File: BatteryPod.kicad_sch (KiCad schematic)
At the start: 15 parts, among them J1 Conn_01x02_Pin, U1 LM5157RTER

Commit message: feat: almost full initial routing
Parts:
- removed J1: Conn_01x02_Pin, Connector_PinHeader_2.54mm:PinHeader_1x02_P2.54mm_Vertical, symbol Connector:Conn_01x02_Pin
- added C8: 100uF, Capacitor_SMD:CP_Elec_16x17.5, symbol Device:C_Polarized
- added H1, H2, H3, H4: MountingHole, MountingHole:MountingHole_2.5mm, symbol Mechanical:MountingHole
- added J1: VIN, Connector_Wire:SolderWire-1.5sqmm_1x02_P7.8mm_D1.7mm_OD3.9mm, symbol Connector:Conn_01x02_Socket
- C2: footprint Capacitor_SMD:C_0603_1608Metric -> Capacitor_SMD:C_2220_5750Metric
- C6: Part C426635 -> C107086
- C7: Part C2986269 -> C307347
- R1: Part (none) -> C234251
- R2: Part (none) -> C491121
- R4: Part C705949 -> C218107
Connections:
- net +BATT: now also J1.1 (Pin_1)
- net GND: now also C8.2, J1.2 (Pin_2)
- net VCC: now reaches C1.1, C4.1, D1.1 (K), R1.1
- net VCC: now also C8.1

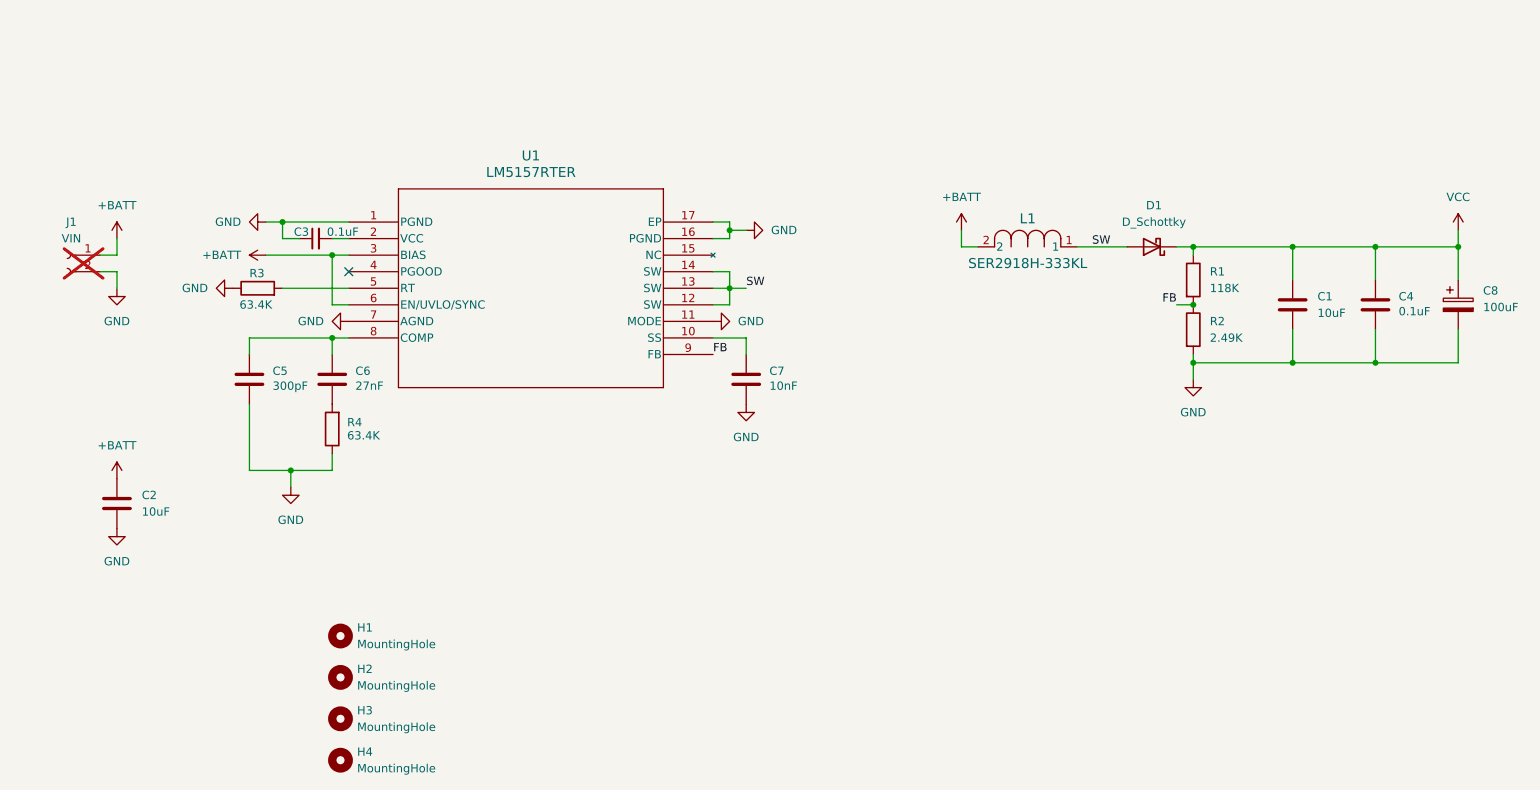
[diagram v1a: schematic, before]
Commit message: feat: correct screw positioning (hopefully)
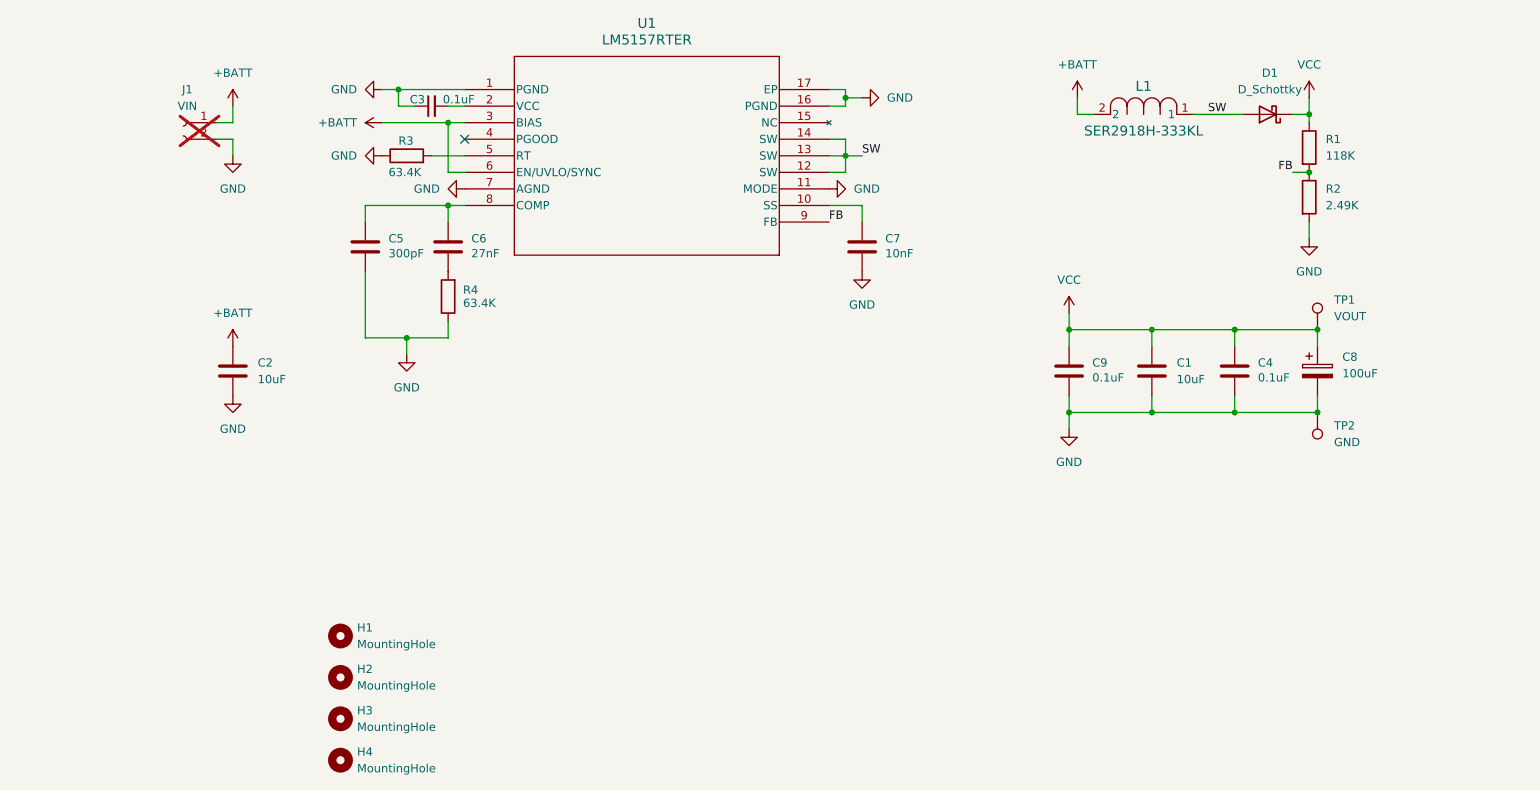
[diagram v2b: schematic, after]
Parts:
- added C9: 0.1uF, Capacitor_SMD:C_0603_1608Metric, symbol Device:C
- added TP1: VOUT, TestPoint:TestPoint_Loop_D2.50mm_Drill1.0mm_LowProfile, symbol Connector:TestPoint
- added TP2: GND, TestPoint:TestPoint_Loop_D2.50mm_Drill1.0mm_LowProfile, symbol Connector:TestPoint
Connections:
- net GND: now also C9.2, TP2.1
- net VCC: now also C9.1, TP1.1
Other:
- moved on the sheet: C2, C3, C5, C6, C7, D1, J1, L1, R1, R2, R3, R4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

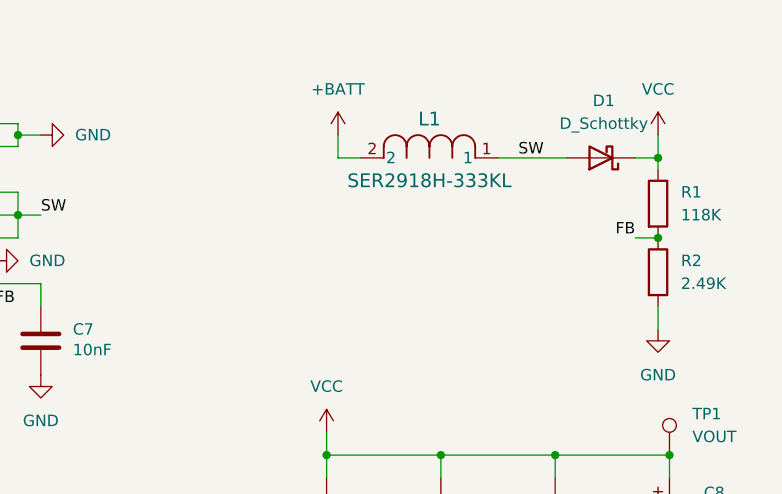
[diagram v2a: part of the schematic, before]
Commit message: patch: silkscreen improvements fix: screw hole position
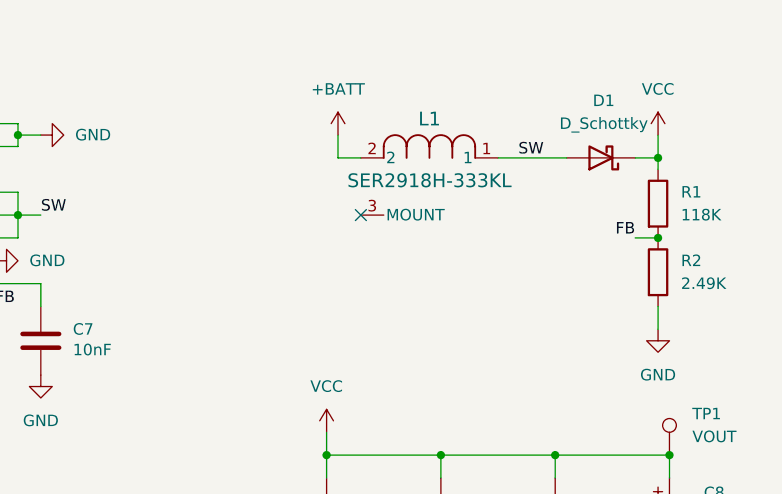
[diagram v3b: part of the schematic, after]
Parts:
- L1: footprint coilcraft-ser2918h:IND_SER2918H_COC -> IND_SER2918H_COC
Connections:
- no-connect marks 1 -> 2
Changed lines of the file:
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@@
 		(at 105.41 83.82)
+	)
+	(no_connect
+		(at 201.93 86.36)
 	)
 	(wire
@@
 			)
 		)
-		(property "Footprint" "coilcraft-ser2918h:IND_SER2918H_COC"
+		(property "Footprint" "IND_SER2918H_COC"
 			(at 201.93 80.01 0)
 			(effects
@@
 		(pin "1"
 		)
+		(pin "3"
+		)
 		(instances

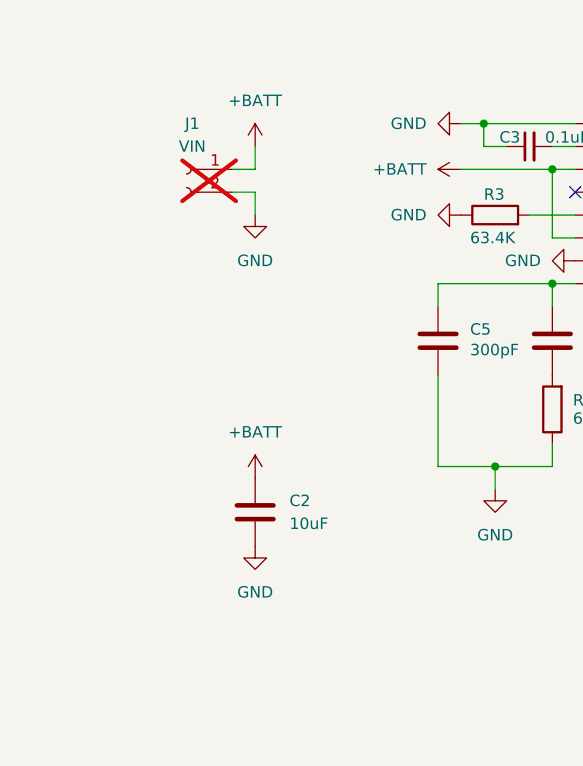
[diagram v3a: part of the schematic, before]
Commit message: feat: move to lower half of board due to high profile inductor this is to match with a recess in the chassis for the higher profile component
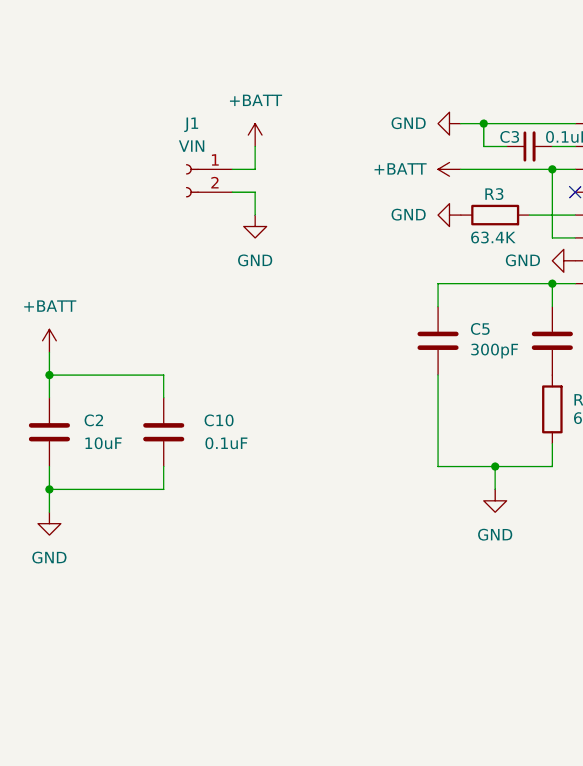
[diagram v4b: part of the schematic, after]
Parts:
- added C10: 0.1uF, Capacitor_SMD:C_0603_1608Metric, symbol Device:C
- C8: footprint Capacitor_SMD:CP_Elec_16x17.5 -> Capacitor_SMD:CP_Elec_10x10; Part C445445 -> C487156
- J1: now fitted; now left out of the parts list
- TP1, TP2: now left out of the parts list
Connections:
- net +BATT: now also C10.2
- net GND: now also C10.1
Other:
- moved on the sheet: C2
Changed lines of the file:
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@@
 	(paper "A4")
 	(junction
+		(at 46.99 104.14)
+		(diameter 0)
+		(color 0 0 0 0)
+	)
+	(junction
 		(at 210.82 125.73)
 		(diameter 0)
@@
 	)
 	(junction
+		(at 46.99 116.84)
+		(diameter 0)
+		(color 0 0 0 0)
+	)
+	(junction
 		(at 210.82 113.03)
 		(diameter 0)
@@
 	(wire
 		(pts
+			(xy 46.99 119.38) (xy 46.99 116.84)
+		)
+		(stroke
+			(width 0)
+			(type default)
+		)
+	)
+	(wire
+		(pts
 			(xy 198.12 110.49) (xy 198.12 113.03)
 		)
@@
 	(wire
 		(pts
+			(xy 46.99 101.6) (xy 46.99 104.14)
+		)
+		(stroke
+			(width 0)
+			(type default)
+		)
+	)
+	(wire
+		(pts
 			(xy 198.12 125.73) (xy 210.82 125.73)
 		)
@@
 	(wire
 		(pts
+			(xy 59.69 116.84) (xy 59.69 114.3)
+		)
+		(stroke
+			(width 0)
+			(type default)
+		)
+	)
+	(wire
+		(pts
 			(xy 234.95 80.01) (xy 234.95 81.28)
 		)
@@
 	(wire
 		(pts
+			(xy 46.99 104.14) (xy 46.99 106.68)
+		)
+		(stroke
+			(width 0)
+			(type default)
+		)
+	)
+	(wire
+		(pts
 			(xy 232.41 88.9) (xy 234.95 88.9)
 		)
@@
 	(wire
 		(pts
+			(xy 59.69 104.14) (xy 59.69 106.68)
+		)
+		(stroke
+			(width 0)
+			(type default)
+		)
+	)
+	(wire
+		(pts
 			(xy 236.22 123.19) (xy 236.22 125.73)
 		)
@@
 	(wire
 		(pts
+			(xy 46.99 116.84) (xy 59.69 116.84)
+		)
+		(stroke
+			(width 0)
+			(type default)
+		)
+	)
+	(wire
+		(pts
 			(xy 210.82 115.57) (xy 210.82 113.03)
 		)
@@
 	(wire
 		(pts
+			(xy 46.99 104.14) (xy 59.69 104.14)
+		)
+		(stroke
+			(width 0)
+			(type default)
+		)
+	)
+	(wire
+		(pts
 			(xy 163.83 78.74) (xy 163.83 77.47)
 		)
@@
 	(wire
 		(pts
+			(xy 46.99 116.84) (xy 46.99 114.3)
+		)
+		(stroke
+			(width 0)
+			(type default)
+		)
+	)
+	(wire
+		(pts
 			(xy 163.83 83.82) (xy 161.29 83.82)
 		)
@@
 	(symbol
 		(lib_id "Device:C")
-		(at 69.85 119.38 0)
+		(at 46.99 110.49 0)
 		(unit 1)
 		(exclude_from_sim no)
@@
 		(fields_autoplaced yes)
 		(property "Reference" "C2"
-			(at 73.66 118.1099 0)
+			(at 50.8 109.2199 0)
 			(effects
 				(font
@@
 		)
 		(property "Value" "10uF"
-			(at 73.66 120.6499 0)
+			(at 50.8 111.7599 0)
 			(effects
 				(font
@@
 		)
 		(property "Footprint" "Capacitor_SMD:C_2220_5750Metric"
-			(at 70.8152 123.19 0)
+			(at 47.9552 114.3 0)
 			(effects
 				(font
@@
 		)
 		(property "Datasheet" "~"
-			(at 69.85 119.38 0)
+			(at 46.99 110.49 0)
 			(effects
 				(font
@@
 		)
 		(property "Description" "Unpolarized capacitor"
-			(at 69.85 119.38 0)
+			(at 46.99 110.49 0)
 			(effects
 				(font
@@
 		)
 		(property "Part" "C342280"
-			(at 69.85 119.38 0)
+			(at 46.99 110.49 0)
 			(effects
 				(font
@@
 		)
 		(property "Part#" ""
-			(at 69.85 119.38 0)
+			(at 46.99 110.49 0)
 			(effects
 				(font
@@
 		(unit 1)
 		(exclude_from_sim no)
-		(in_bom yes)
+		(in_bom no)
 		(on_board yes)
 		(dnp no)
@@
 			)
 		)
-		(property "Part#" ""
-			(at 100.33 78.74 0)
-			(effects
-				(font
-					(size 1.27 1.27)
-				)
-				(hide yes)
-			)
-		)
 		(pin "1"
 		)
@@
 		(unit 1)
 		(exclude_from_sim no)
-		(in_bom yes)
+		(in_bom no)
 		(on_board yes)
-		(dnp yes)
+		(dnp no)
 		(fields_autoplaced yes)
 		(property "Reference" "J1"
@@
 		(unit 1)
 		(exclude_from_sim no)
-		(in_bom yes)
+		(in_bom no)
 		(on_board yes)
 		(dnp no)
@@
 	(symbol
 		(lib_id "power:+BATT")
-		(at 69.85 115.57 0)
+		(at 46.99 101.6 0)
 		(unit 1)
 		(exclude_from_sim no)
@@
 		(fields_autoplaced yes)
 		(property "Reference" "#PWR010"
-			(at 69.85 119.38 0)
+			(at 46.99 105.41 0)
 			(effects
 				(font
@@
 		)
 		(property "Value" "+BATT"
-			(at 69.85 110.49 0)
+			(at 46.99 96.52 0)
 			(effects
 				(font
@@
 		)
 		(property "Footprint" ""
-			(at 69.85 115.57 0)
+			(at 46.99 101.6 0)
 			(effects
 				(font
@@
 		)
 		(property "Datasheet" ""
-			(at 69.85 115.57 0)
+			(at 46.99 101.6 0)
 			(effects
 				(font
@@
 		)
 		(property "Description" "Power symbol creates a global label with name \"+BATT\""
-			(at 69.85 115.57 0)
+			(at 46.99 101.6 0)
 			(effects
 				(font
@@
 	(symbol
 		(lib_id "power:GND")
-		(at 69.85 123.19 0)
+		(at 46.99 119.38 0)
 		(unit 1)
 		(exclude_from_sim no)
@@
 		(fields_autoplaced yes)
 		(property "Reference" "#PWR011"
-			(at 69.85 129.54 0)
+			(at 46.99 125.73 0)
 			(effects
 				(font
@@
 		)
 		(property "Value" "GND"
-			(at 69.85 128.27 0)
+			(at 46.99 124.46 0)
 			(effects
 				(font
@@
 		)
 		(property "Footprint" ""
-			(at 69.85 123.19 0)
+			(at 46.99 119.38 0)
 			(effects
 				(font
@@
 		)
 		(property "Datasheet" ""
-			(at 69.85 123.19 0)
+			(at 46.99 119.38 0)
 			(effects
 				(font
@@
 		)
 		(property "Description" "Power symbol creates a global label with name \"GND\" , ground"
-			(at 69.85 123.19 0)
+			(at 46.99 119.38 0)
 			(effects
 				(font
@@
 	)
 	(symbol
+		(lib_id "Device:C")
+		(at 59.69 110.49 180)
+		(unit 1)
+		(exclude_from_sim no)
+		(in_bom yes)
+		(on_board yes)
+		(dnp no)
+		(property "Reference" "C10"
+			(at 67.564 109.22 0)
+			(effects
+				(font
+					(size 1.27 1.27)
+				)
+				(justify left)
+			)
+		)
+		(property "Value" "0.1uF"
+			(at 69.088 111.76 0)
+			(effects
+				(font
+					(size 1.27 1.27)
+				)
+				(justify left)
+			)
+		)
+		(property "Footprint" "Capacitor_SMD:C_0603_1608Metric"
+			(at 58.7248 106.68 0)
+			(effects
+				(font
+					(size 1.27 1.27)
+				)
+				(hide yes)
+			)
+		)
+		(property "Datasheet" "~"
+			(at 59.69 110.49 0)
+			(effects
+				(font
+					(size 1.27 1.27)
+				)
+				(hide yes)
+			)
+		)
+		(property "Description" "Unpolarized capacitor"
+			(at 59.69 110.49 0)
+			(effects
+				(font
+					(size 1.27 1.27)
+				)
+				(hide yes)
+			)
+		)
+		(property "Part" "C597287"
+			(at 59.69 110.49 90)
+			(effects
+				(font
+					(size 1.27 1.27)
+				)
+				(hide yes)
+			)
+		)
+		(pin "1"
+		)
+		(pin "2"
+		)
+		(instances
+			(project "BatteryPod"
+				(path "/4321c496-0c88-4f4f-a1d3-dd2bca7d98aa"
+					(reference "C10")
+					(unit 1)
+				)
+			)
+		)
+	)
+	(symbol
 		(lib_id "Device:D_Schottky")
 		(at 228.6 80.01 180)
@@
 			)
 		)
-		(property "Footprint" "Capacitor_SMD:CP_Elec_16x17.5"
+		(property "Footprint" "Capacitor_SMD:CP_Elec_10x10"
 			(at 237.1852 123.19 0)
 			(effects
@@
 			)
 		)
-		(property "Part" "C445445"
-			(at 236.22 119.38 0)
-			(effects
-				(font
-					(size 1.27 1.27)
-				)
-				(hide yes)
-			)
-		)
-		(property "Part#" ""
+		(property "Part" "C487156"
 			(at 236.22 119.38 0)
 			(effects

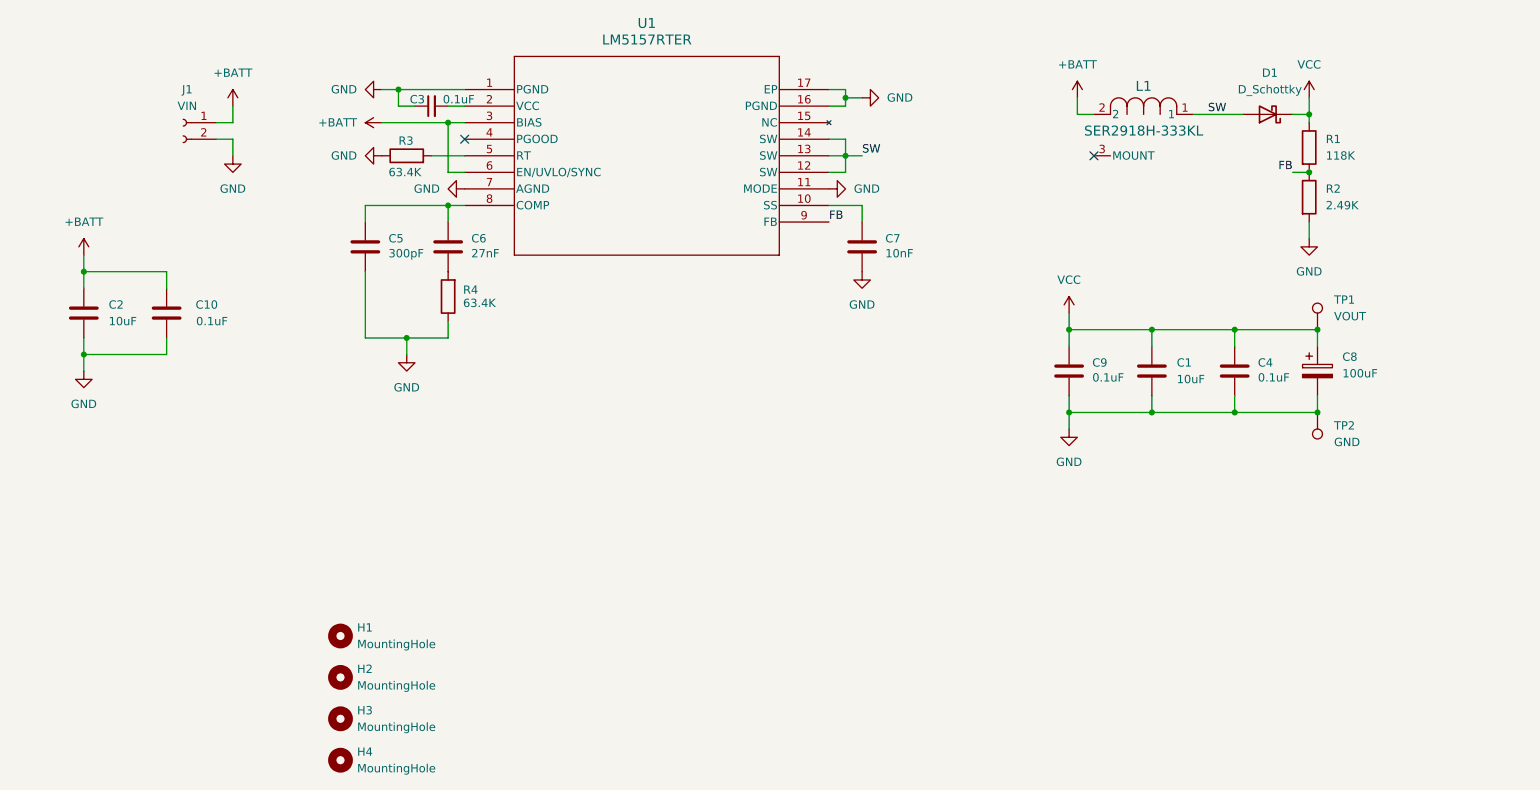
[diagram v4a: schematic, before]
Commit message: feat: add partial USB-PD input, routing
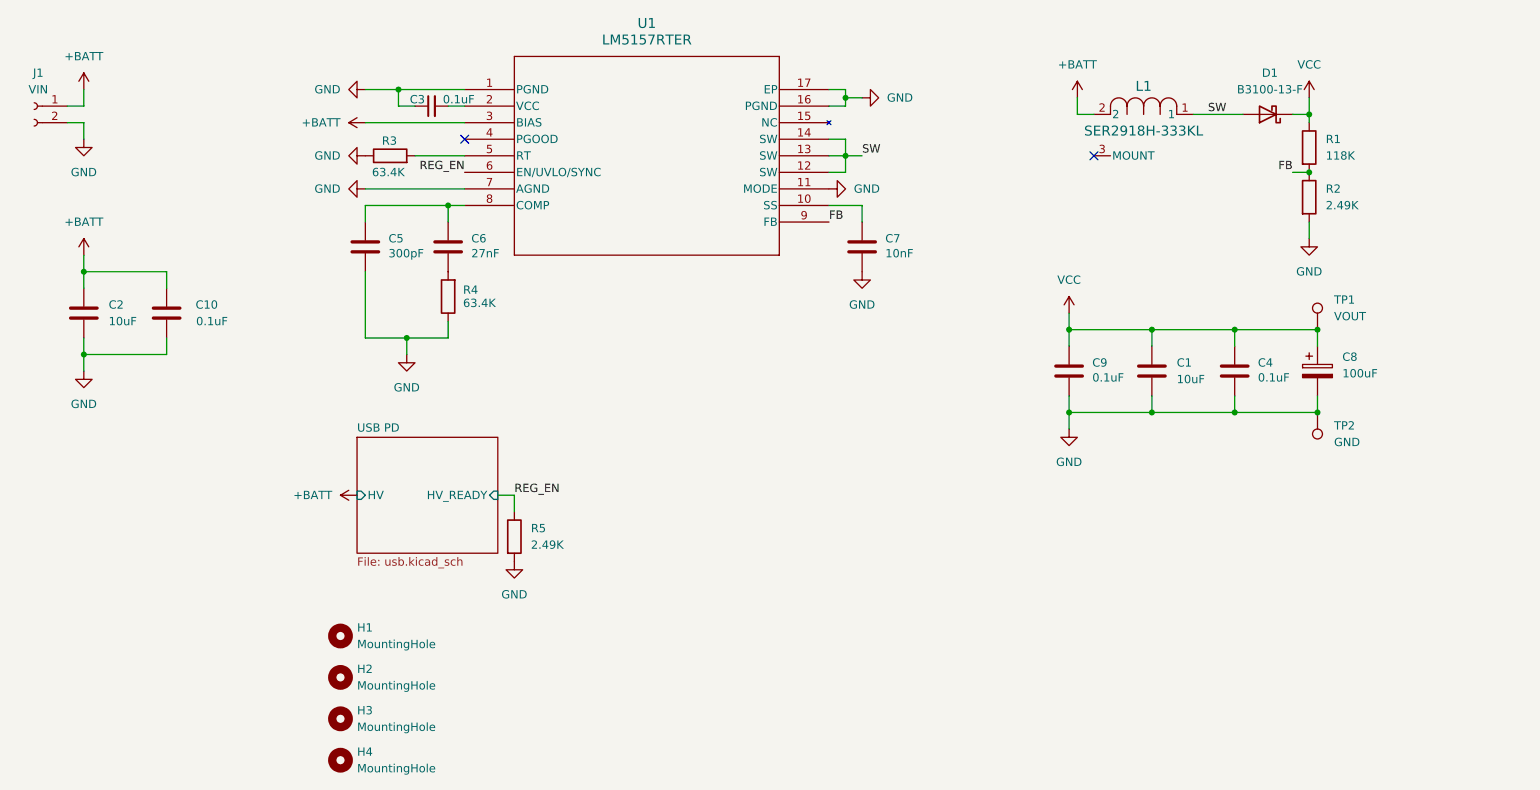
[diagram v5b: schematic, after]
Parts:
- added R5: 2.49K, Resistor_SMD:R_0603_1608Metric, symbol Device:R
- D1: value D_Schottky -> B3100-13-F
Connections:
- net +BATT: no longer U1.6 (EN/UVLO/SYNC)
- net GND: now also R5.2
- new net REG_EN: R5.1, U1.6 (EN/UVLO/SYNC)
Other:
- added sheet USB PD (usb.kicad_sch)
- moved on the sheet: J1, R3
